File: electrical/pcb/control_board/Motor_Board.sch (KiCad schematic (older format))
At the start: 84 parts, among them J1 XT30-M, J10 Molex_172675-0613, J11 Molex_172675-0613, J12 TSW-104-07-F-T, J13 Molex_172675-0613, J14 Molex_172675-0613, J15 TSW-104-07-F-T, J16 277-11404-ND, J17 277-11404-ND, J18 277-11404-ND, J19 TSW-104-07-F-T, J2 XT30-F, J20 PEC08SAAN, J21 PPTC102LFBN-RC, J3 XT30-F, J4 XT30-F, J5 XT30-M, J6 ED2580-ND, J7 TSW-104-07-F-T, J8 Molex_172675-0613, J9 Molex_172675-0613, T1 test_point, T10 test_point, T11 test_point, T12 test_point, T2 test_point, T3 test_point, T4 test_point, T5 test_point, T6 test_point, T7 test_point, T8 test_point, T9 test_point, U1 INA260, U2 PCA9685, U3 D24V22Fx, U4 D24V150Fx, U5 DC7G3HWA, y1 rover_silkscreen

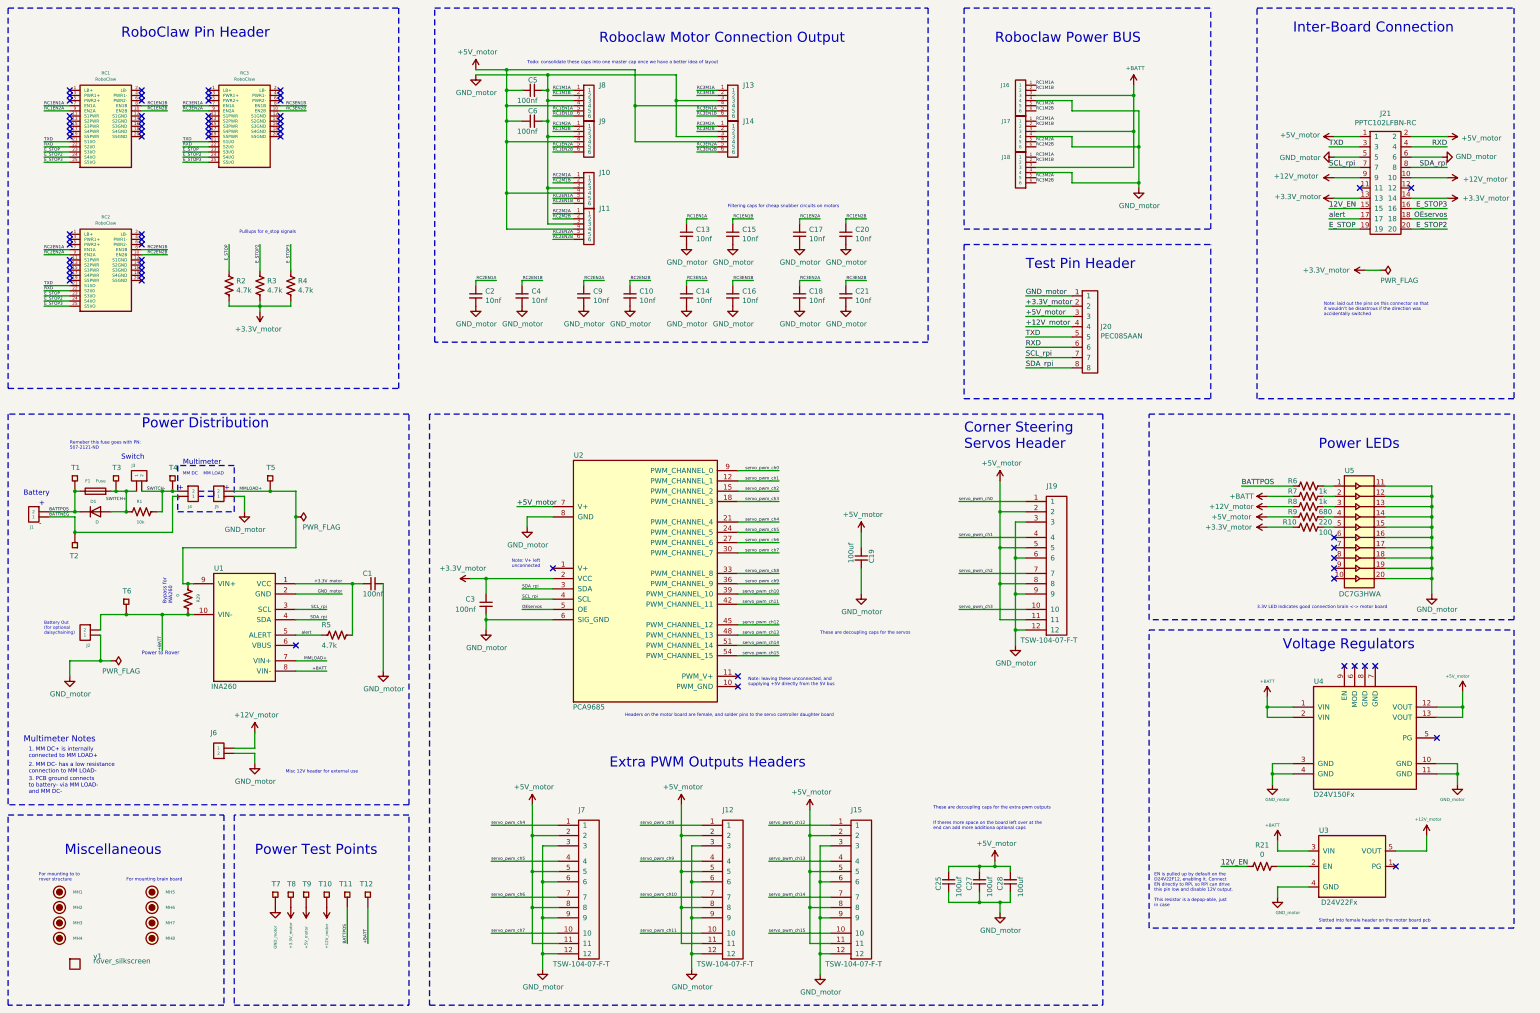
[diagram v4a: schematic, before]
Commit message: Moved alert LED to motor board, and moved estop pulldowns to have as an "option 2"
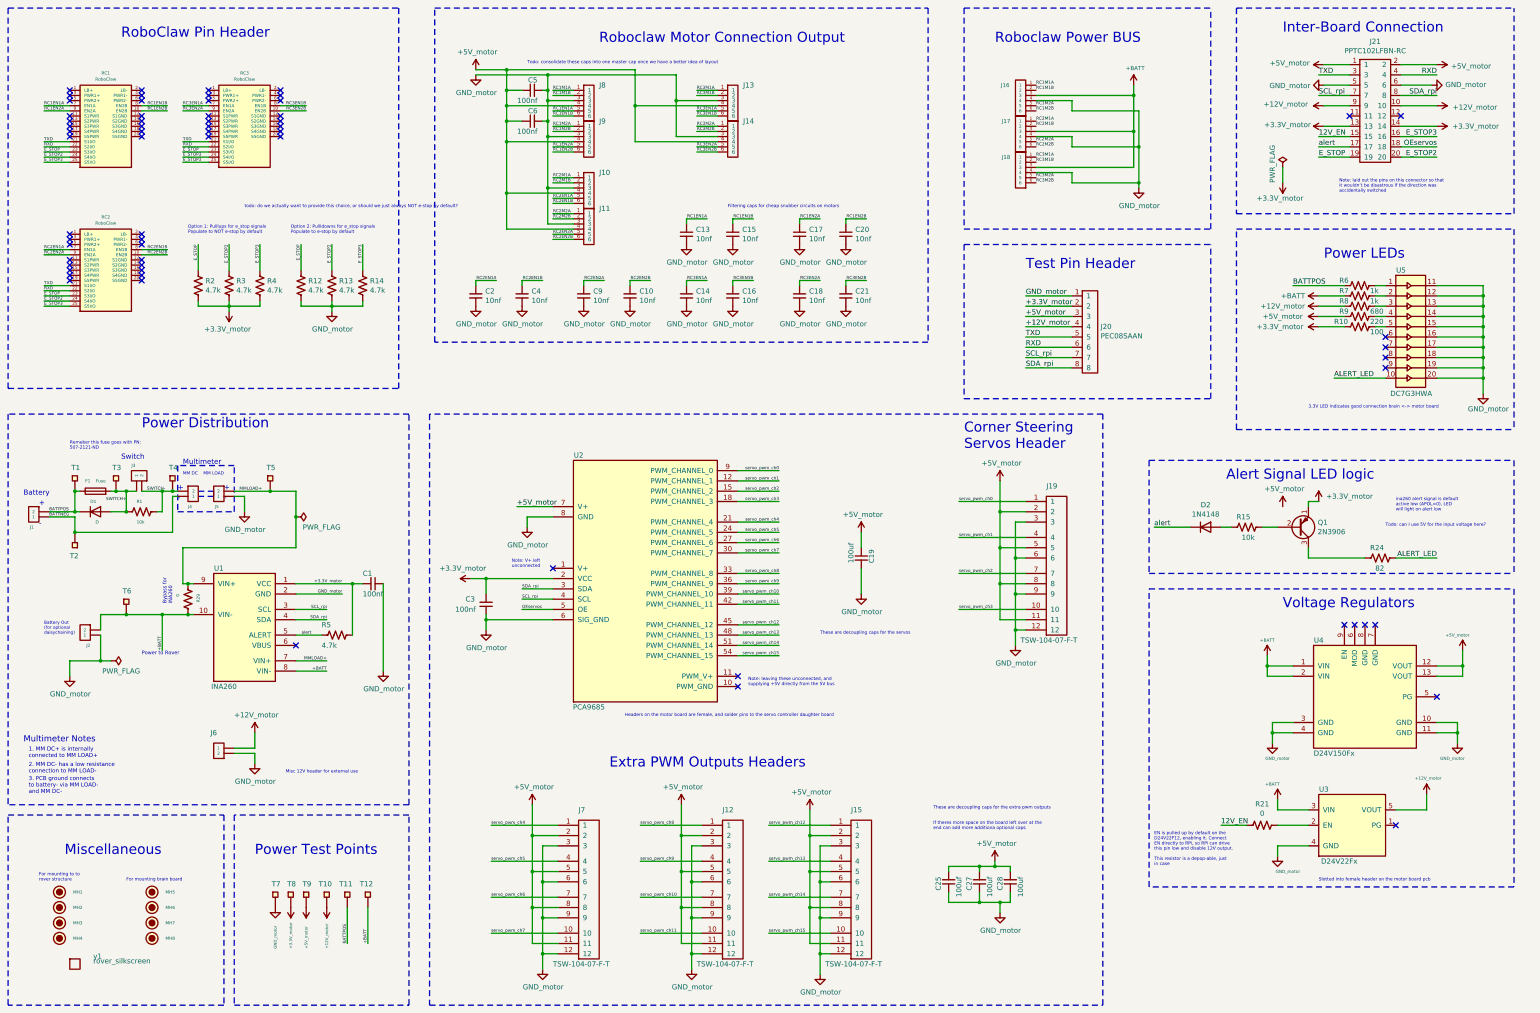
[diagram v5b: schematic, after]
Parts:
- added D2: 1N4148, Diode_THT:D_DO-35_SOD27_P7.62mm_Horizontal, symbol Diode:1N4148
- added Q1: 2N3906, Package_TO_SOT_THT:TO-92_Inline, symbol Transistor_BJT:2N3906
- added R12, R13, R14: 4.7k, Resistor_THT:R_Axial_DIN0207_L6.3mm_D2.5mm_P7.62mm_Horizontal, symbol Device:R_US
- added R15: 10k, Resistor_THT:R_Axial_DIN0207_L6.3mm_D2.5mm_P7.62mm_Horizontal, symbol Device:R_US
- added R24: 82, Resistor_THT:R_Axial_DIN0207_L6.3mm_D2.5mm_P7.62mm_Horizontal, symbol Device:R_US
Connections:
- net +3.3V_motor: now also Q1.1 (E)
- net E_STOP: now also R12.1
- net E_STOP2: now also R13.1
- net E_STOP3: now also R14.1
- net GND_motor: now also R12.2, R13.2, R14.2
- net alert: now also D2.1 (K)
- net ALERT_LED: now reaches U5.10
- net ALERT_LED: now also R24.1
- new net: Q1.2 (B), R15.1
- new net: D2.2 (A), R15.2
- new net: Q1.3 (C), R24.2
- no-connect marks 65 -> 64
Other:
- note added: "Alert Signal LED logic"
- note added: "Option 1: Pulllups for e_stop signals\nPopulate to NOT e-stop by default"
- note added: "Option 2: Pullldowns for e_stop signals\nPopulate to e-stop by default"
- note added: "Todo: can I use 5V for the input voltage here?"
- note added: "ina260 alert signal is default \nactive low (APOL=0), LED \nwill light on alert low"
- note added: "todo: do we actually want to provide this choice, or should we just always NOT e-stop by default?"
- note removed: "Pulllups for e_stop signals"
- moved on the sheet: J21, R10, R2, R21, R3, R4, R6, R7, R8, R9, U3, U4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

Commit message: adding some notes from thursday convo
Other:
- note added: "todo: this 3.3v motor led needs to be done like the brain board"
- note removed: "Todo: consolidate these caps into one master cap once we have a better idea of layout"
- note removed: "todo: do we actually want to provide this choice, or should we just always NOT e-stop by default?"
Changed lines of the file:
@@
 Text Notes 13650 4850 0    31   ~ 0
 3.3V LED indicates good connection brain <-> motor board
-Text Notes 6050 1500 0    31   ~ 0
-Todo: consolidate these caps into one master cap once we have a better idea of layout
 $Comp
 L JPL_Robotics_Lib:D24V22Fx U3
@@
 	1    0    0    -1
 $EndComp
-Text Notes 3300 2900 0    31   ~ 0
-todo: do we actually want to provide this choice, or should we just always NOT e-stop by default?
+Text Notes 12900 4650 0    31   ~ 0
+todo: this 3.3v motor led needs to be done like the brain board
 $EndSCHEMATC

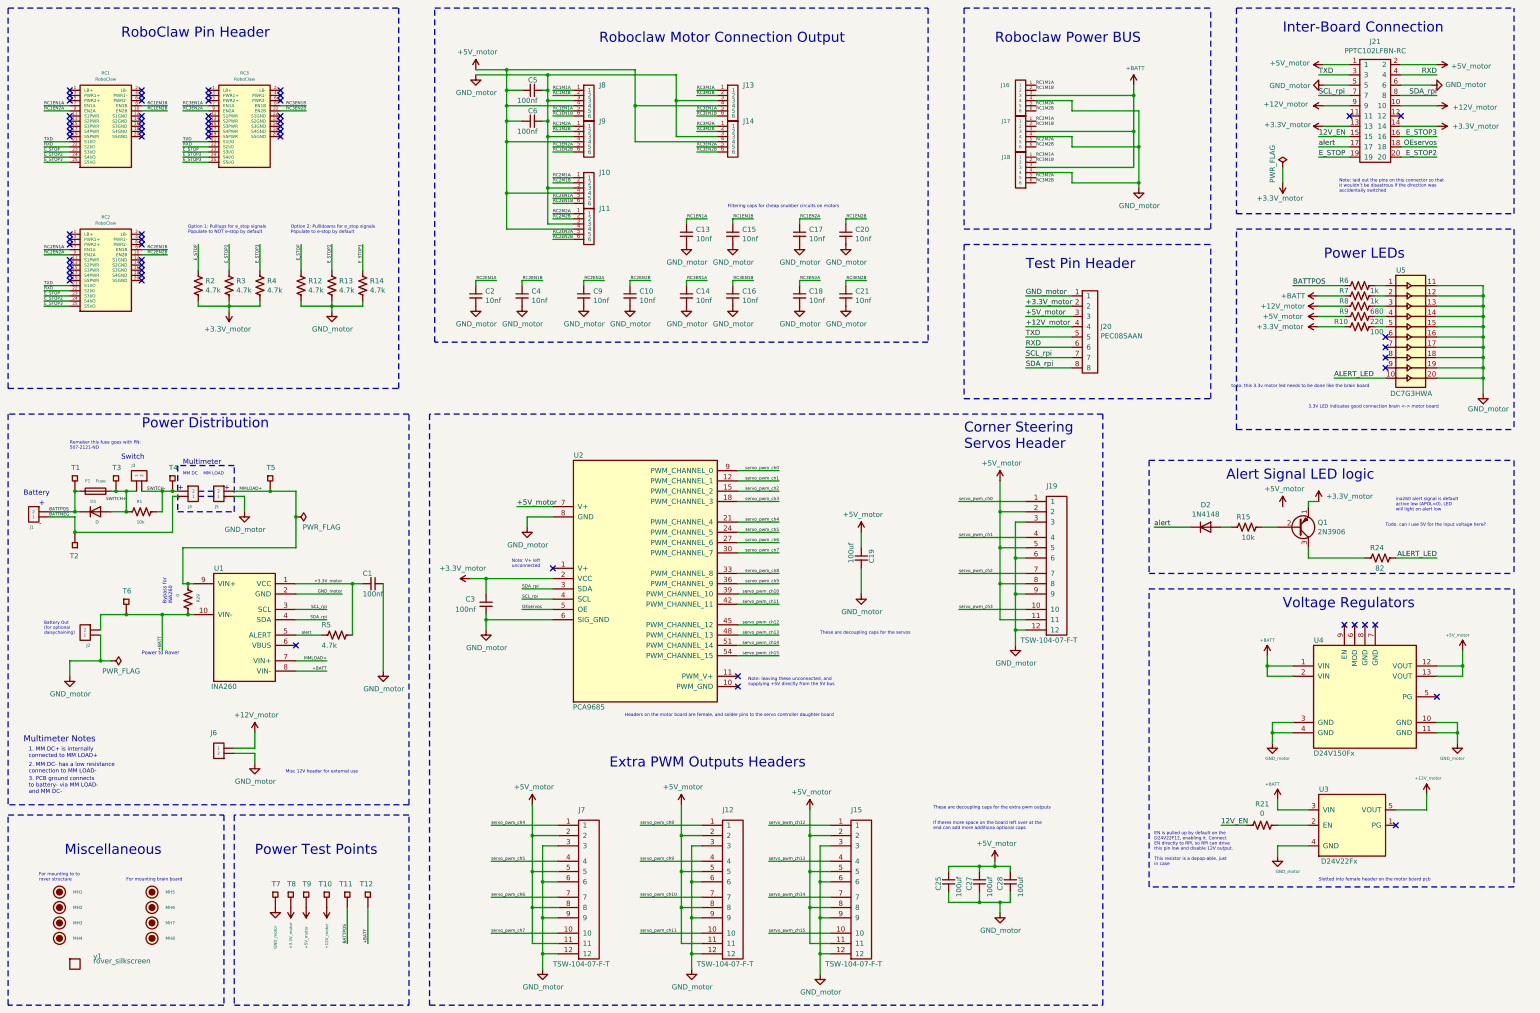
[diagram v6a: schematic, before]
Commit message: Overhauled 3.3v rail and updated LEDs to use it
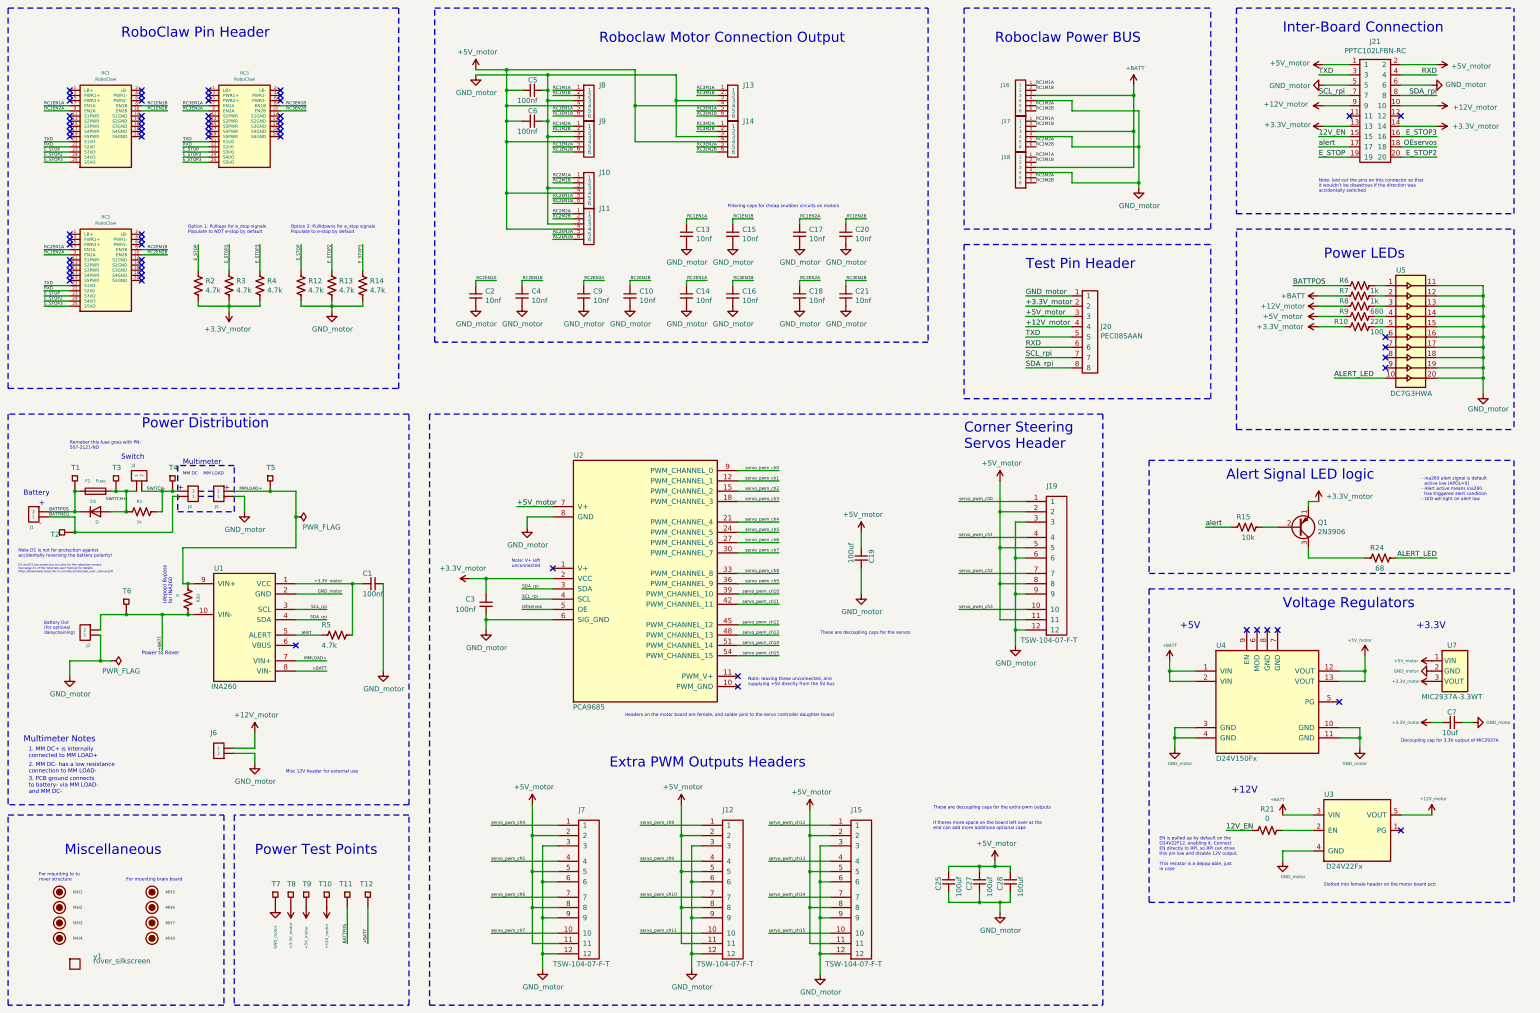
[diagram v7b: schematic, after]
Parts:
- removed D2: 1N4148, Diode_THT:D_DO-35_SOD27_P7.62mm_Horizontal, symbol Diode:1N4148
- added C7: 10uf, Capacitor_THT:CP_Radial_D8.0mm_P3.80mm, symbol Device:C_Small
- added U7: MIC2937A-3.3WT, Package_TO_SOT_THT:TO-220-3_Vertical, symbol JPL_Robotics_Lib:MIC2937A-3.3WT
- R1: value 10k -> 1k
- R24: value 82 -> 68
- renumbered R29 to R30
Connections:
- net +3.3V_motor: now also C7.2, U7.3 (VOUT)
- net +5V_motor: now also U7.1 (VIN)
- net GND_motor: now also C7.1, U7.2 (GND)
- net alert: now also R15.2
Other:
- note added: "(depop) Bypass \nfor INA260\n"
- note added: "+12V\n"
- note added: "+3.3V\n"
- note added: "+5V\n"
- note added: "- ina260 alert signal is default \n active low (APOL=0)\n- Alert active means ina260 \n has triggered alert condition\n- LED will light on alert low"
- note added: "D1 and R1 are protective circuitry for the roboclaw motors. \nSee page 41 of the roboclaw user manual for details: \nhttps://downloads.basicmicro.com/docs/roboclaw_user_manual.pdf"
- note added: "Decoupling cap for 3.3V output of MIC2937A"
- note added: "Note D1 is not for protection against\naccidentally reversing the battery polarity!"
- note removed: "3.3V LED indicates good connection brain <-> motor board"
- note removed: "Bypass for \nINA260\n"
- note removed: "Todo: can I use 5V for the input voltage here?"
- note removed: "ina260 alert signal is default \nactive low (APOL=0), LED \nwill light on alert low"
- note removed: "todo: this 3.3v motor led needs to be done like the brain board"
- moved on the sheet: R21, T2, U3, U4
